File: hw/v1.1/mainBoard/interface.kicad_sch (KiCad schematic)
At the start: 28 parts, among them J1 PWR_LIGHT, J2 I2C, J3 PWR_LIGHT, J5 I2C, J8 PMS5003, Q3 AO3401A, Q4 2N7002, Q7 2N7002, Q8 2N7002, U11 NCP115ASN180T2G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

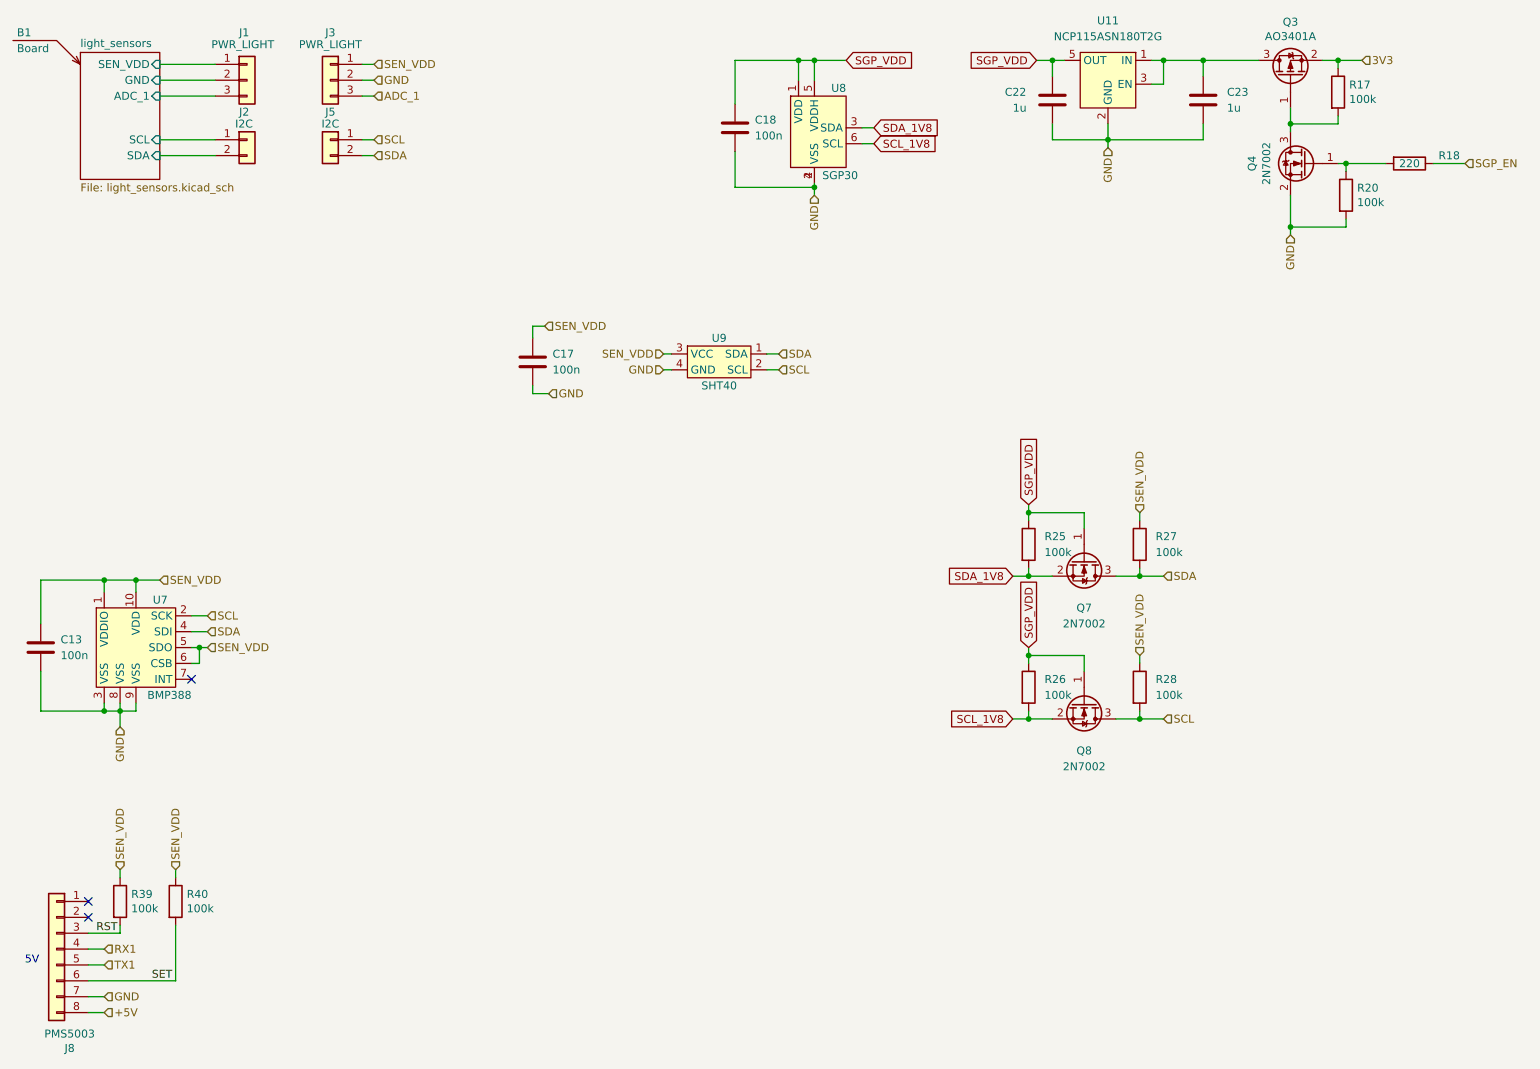
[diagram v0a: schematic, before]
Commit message: Beautify schematics in KiCad
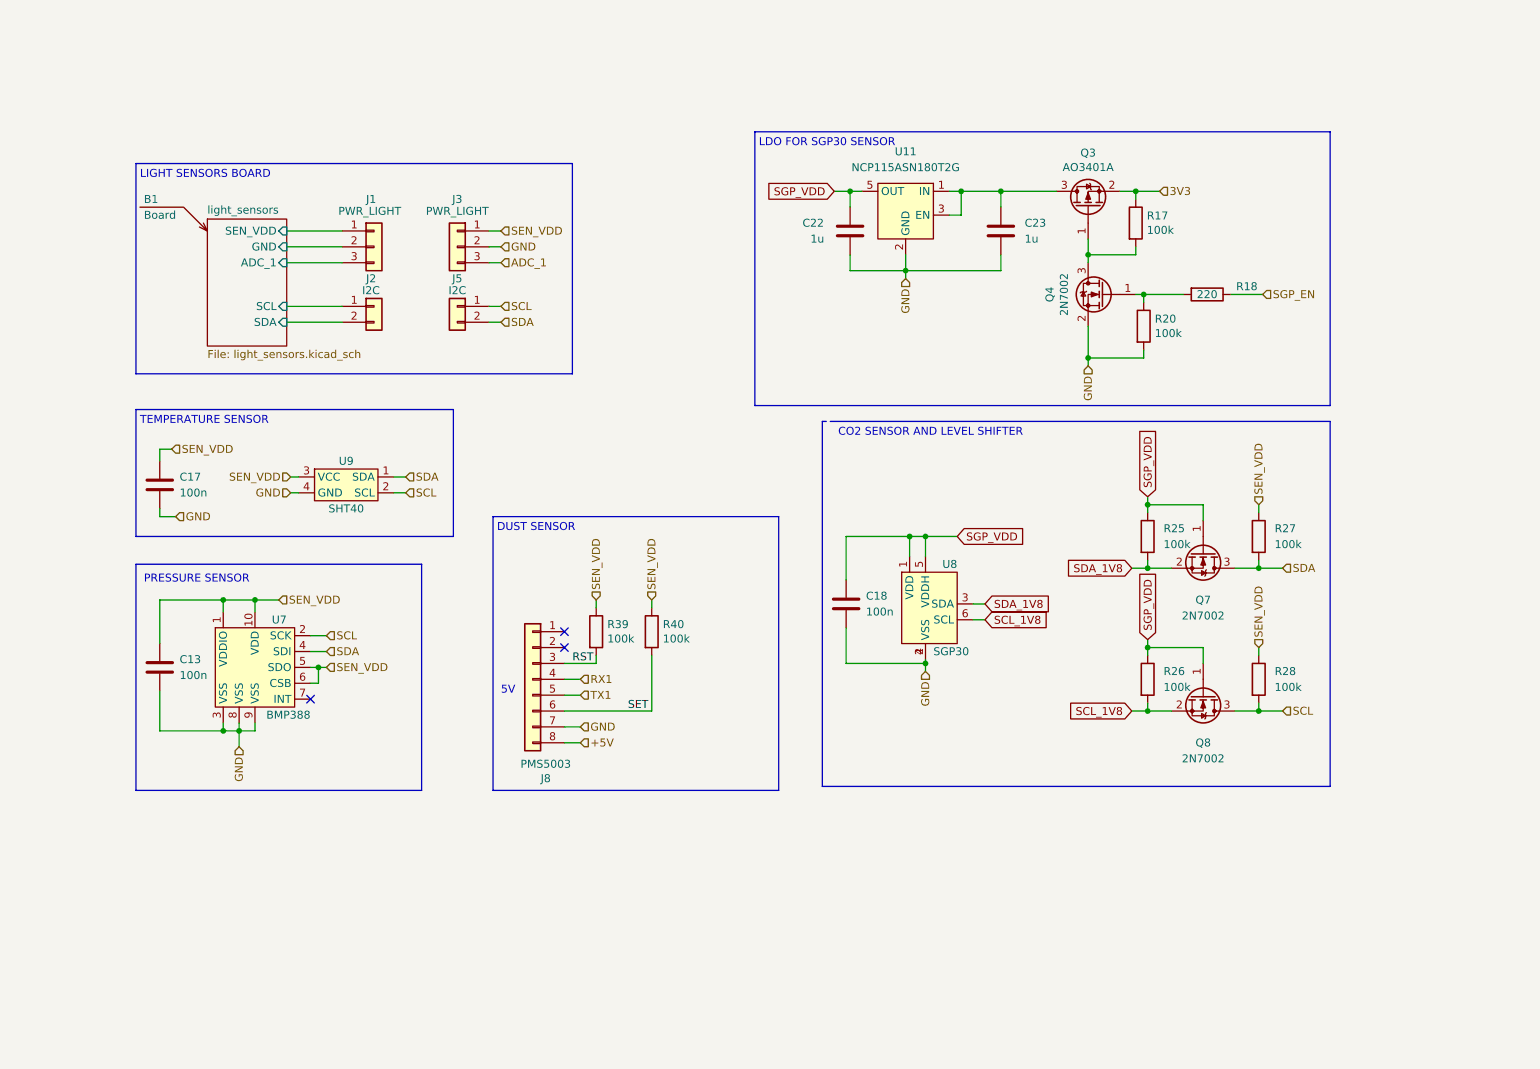
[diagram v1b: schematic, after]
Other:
- note added: "CO2 SENSOR AND LEVEL SHIFTER"
- note added: "DUST SENSOR"
- note added: "LDO FOR SGP30 SENSOR"
- note added: "LIGHT SENSORS BOARD"
- note added: "PRESSURE SENSOR"
- note added: "TEMPERATURE SENSOR"
- company: (none) -> Martin Kousal
- moved on the sheet: B1, C13, C17, C18, C22, C23, J1, J2, J3, J5, J8, Q3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
